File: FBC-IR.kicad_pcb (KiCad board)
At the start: 2 copper layers, 29.3 x 16.3 mm, 18 parts, among them J1 IR LED, J2 IR LED, J3 IR LED, J4 IR LED, Q1 BC850W, Q2 BC850W

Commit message: Add files via upload
Added CPU connection footprints and LED solder pad footprints
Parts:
- added J5: Conn_01x04_Pin, Customs:CPU_connector, F.Cu at (145.6, 89.8)
- J1, J2, J3, J4: footprint Connector_Wire:SolderWirePad_1x01_SMD_1x2mm -> Customs:LED_pad
- moved J4 1.40 mm to (118.7, 84.2)
- moved J2 0.89 mm to (118.7, 86.5)
- moved J3 0.89 mm to (118.7, 85.0)
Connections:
- net CPU_46 renamed /CPU_46
- net CPU_47 renamed /CPU_47
- net CPU_48 renamed /CPU_48
- Q1 pad 1: CPU_45 -> /CPU_45
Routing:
- net /CPU_45: track 0.00 -> 31.9 mm
- net CPU_45: track 29.9 -> 0.00 mm
- net /CPU_48: track 24.8 -> 26.7 mm
- net /CPU_46: track 29.1 -> 30.8 mm
- net /CPU_47: track 27.1 -> 28.7 mm
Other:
- board size 29.3 x 16.3 mm -> 32.9 x 17.8 mm

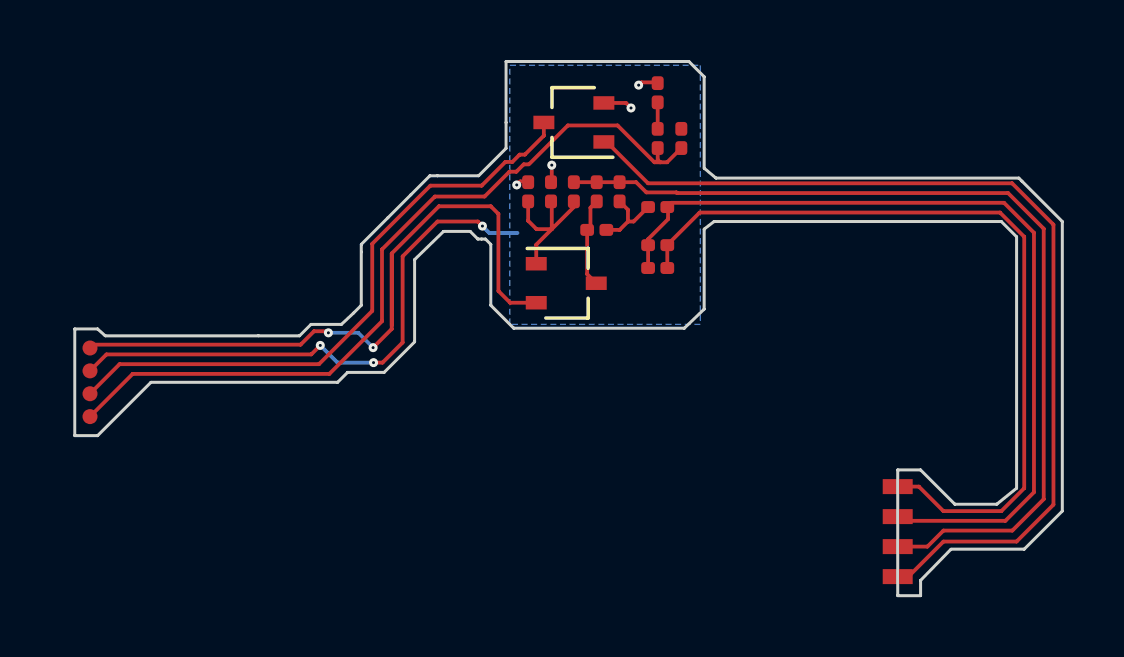
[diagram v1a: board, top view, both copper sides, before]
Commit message: Add files via upload
Fixed CPU connectors causing DRC error. Replaced LED pads with a 1x4 footprint. Fixed Q1 and Q2 footprints not matching prior footprint due to kicad 8.0 upgrade
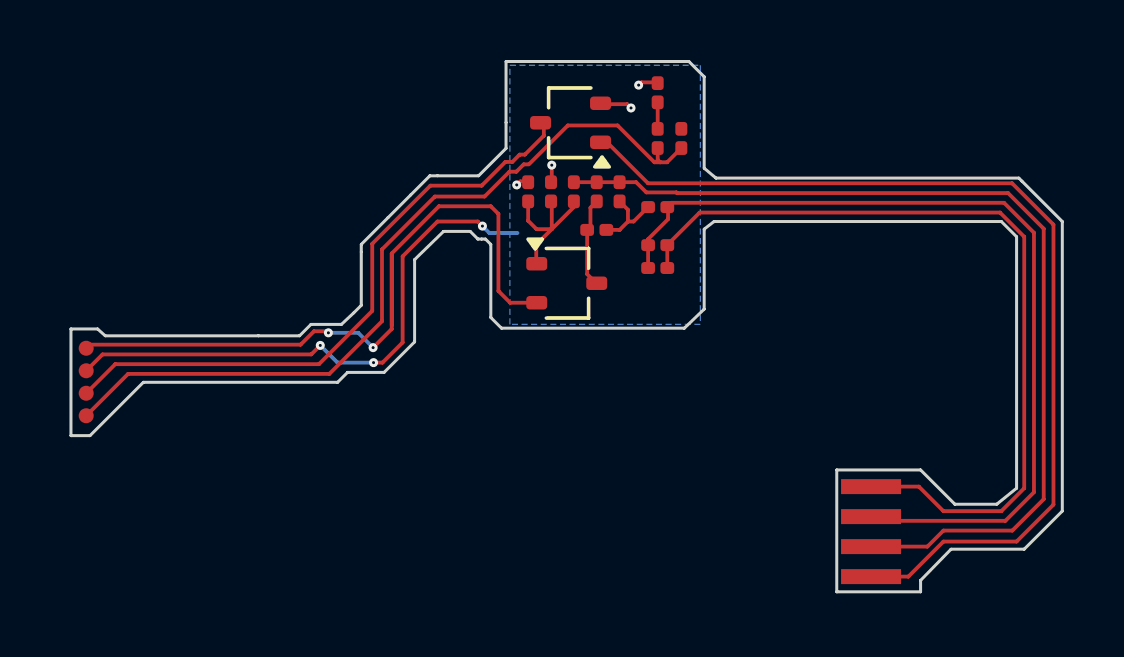
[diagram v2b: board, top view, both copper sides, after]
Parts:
- removed J1, J2, J3, J4: IR LED, Customs:LED_pad
- added J6: Conn_01x04_Pin, Customs:LED_pad, F.Cu at (118.6, 84.7)
- moved J5 0.89 mm to (144.8, 89.8)
- moved Q1 0.11 mm to (134.7, 76.7)
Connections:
- net Net-(J2-Pin_1) renamed /IR_2
- Q1 pad 3: Net-(J1-Pin_1) -> /IR_1
- Q2 pad 2: Net-(J4-Pin_1) -> /PT_2
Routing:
- net /PT_2: track 0.00 -> 24.1 mm, vias 0 -> 2
- net Net-(J4-Pin_1): track 24.0 -> 0.00 mm, vias 2 -> 0
- net /IR_1: track 0.00 -> 20.6 mm
- net Net-(J1-Pin_1): track 20.4 -> 0.00 mm
- net /CPU_47: track 28.7 -> 29.5 mm
- net /CPU_48: track 26.7 -> 27.6 mm
- net /CPU_46: track 30.8 -> 31.7 mm
- net /CPU_45: track 31.9 -> 32.8 mm
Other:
- board size 32.9 x 17.8 mm -> 33 x 17.7 mm
